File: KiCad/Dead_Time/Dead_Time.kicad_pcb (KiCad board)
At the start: 2 copper layers, 13 parts, among them Q7 PNP_BC558, U1 74AUC2G04, U2 Opamp_Dual

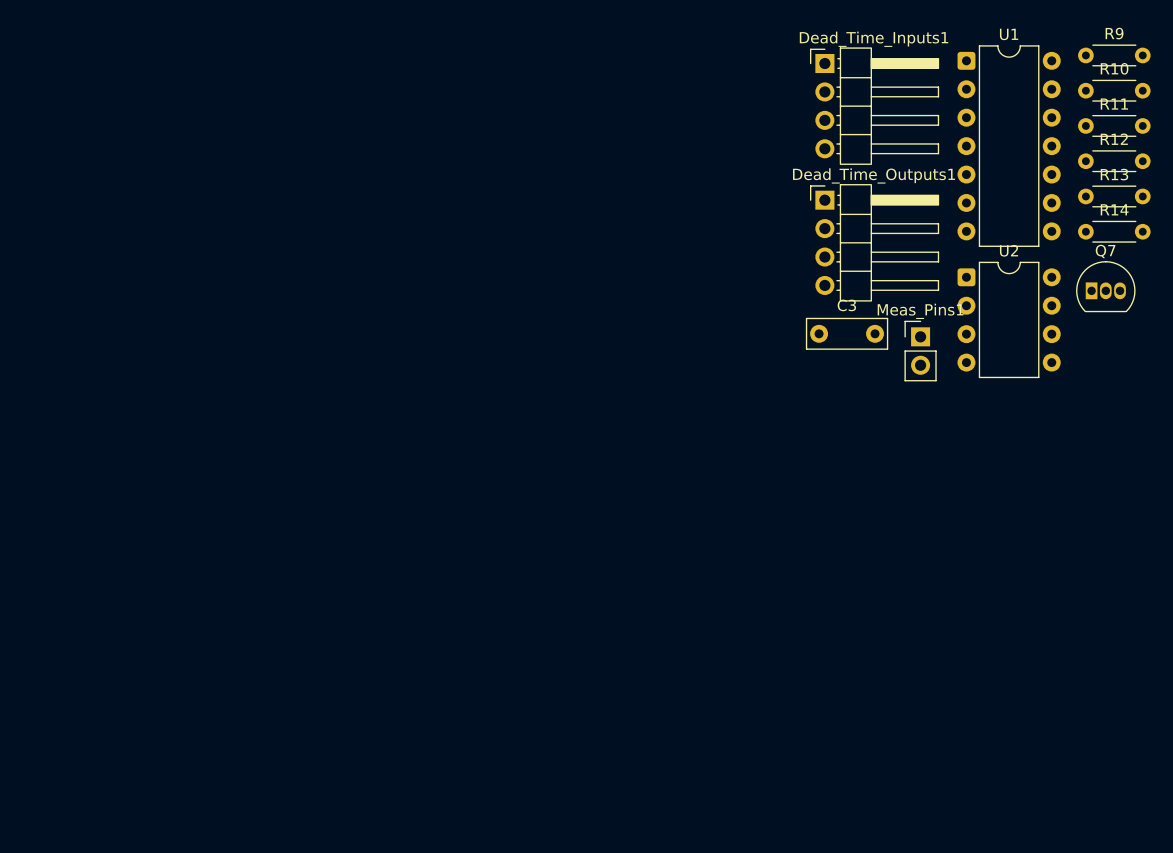
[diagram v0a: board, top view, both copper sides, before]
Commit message: deadtime pcb almost done, missing 1 gnd connection
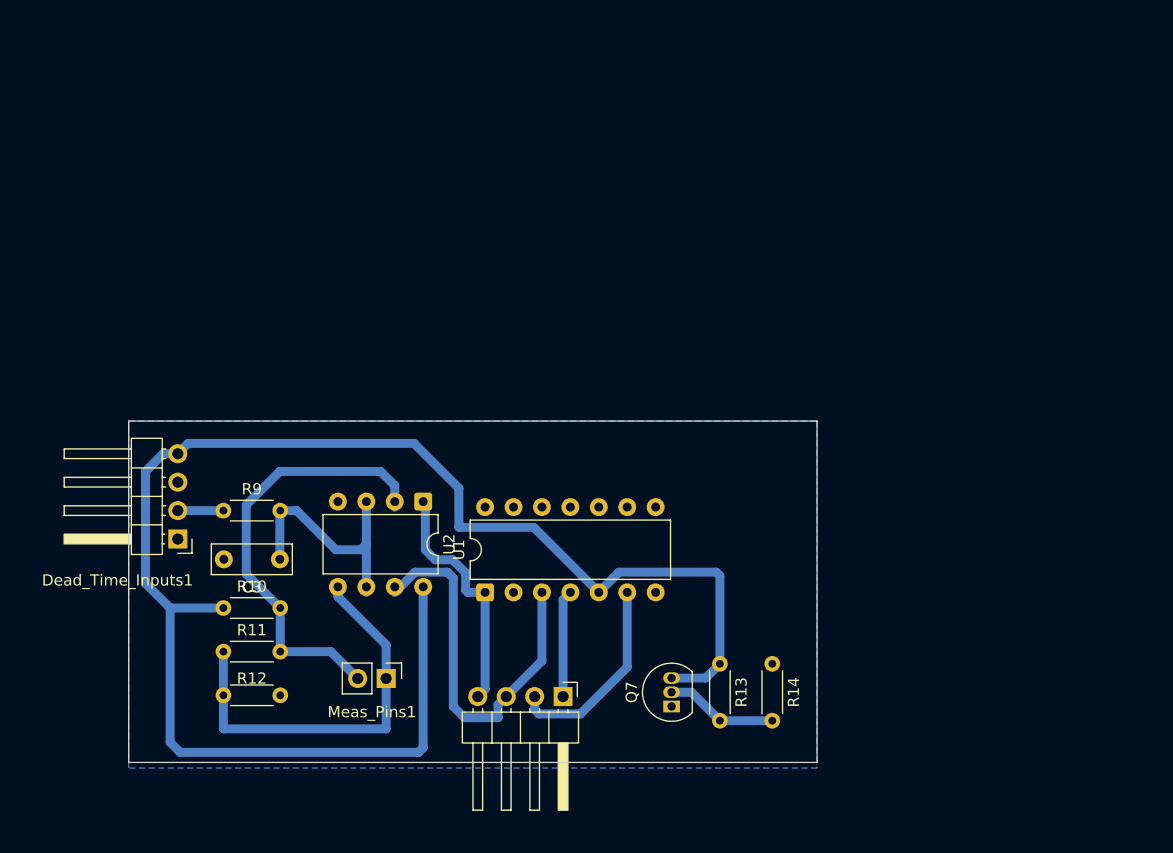
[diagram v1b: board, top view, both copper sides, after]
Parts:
- U2: value Opamp_Dual -> MCP6002
- moved R11 90.2 mm to (85.5, 118.6)
- moved R10 89.9 mm to (85.5, 114.7)
- moved R9 87.1 mm to (85.5, 106.0)
- moved R12 86.4 mm to (90.5, 122.5), turned to 180 degrees
- moved Dead_Time_Inputs1 71.7 mm to (81.4, 108.5), turned to 180 degrees
- moved U1 64.1 mm to (108.8, 113.3), turned to 90 degrees
- moved Meas_Pins1 56.7 mm to (100.0, 121.0), turned to -90 degrees
- moved R13 53.0 mm to (129.8, 119.7), turned to -90 degrees
- moved Q7 52.8 mm to (125.5, 123.5), turned to 90 degrees
- moved U2 52.5 mm to (103.3, 105.2), turned to -90 degrees
- moved C3 52.2 mm to (90.5, 110.3), turned to 180 degrees
- moved Dead_Time_Outputs1 50.1 mm to (115.8, 122.6), turned to -90 degrees
- moved R14 47.7 mm to (134.5, 119.7), turned to -90 degrees
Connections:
- U2 pad 4: (no net) -> GND
- U2 pad 8: (no net) -> +5V
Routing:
- net +5V: track 0.00 -> 140.9 mm
- net /Meas_VStep1: track 0.00 -> 39.2 mm
- net /Meas_VStep2: track 0.00 -> 35.8 mm
- net /PWM2: track 0.00 -> 34.9 mm
- net /PWM1: track 0.00 -> 21.5 mm
- net Net-(U2A-+): track 0.00 -> 21.3 mm
- net /PWM1_NOT: track 0.00 -> 18.0 mm
- net Net-(Q7-B): track 0.00 -> 10.1 mm
- net /PWM2_NOT: track 0.00 -> 9.58 mm
- net /PWM_In: track 0.00 -> 4.46 mm
- added copper zone on B.Cu, net GND
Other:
- board outline added: 61.5 x 30.5 mm

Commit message: gemme punkt før jeg laver om i deadtime pcb
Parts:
- moved Dead_Time_Inputs1 28.9 mm to (108.8, 99.6), turned to 90 degrees
- moved Dead_Time_Outputs1 0.65 mm to (116.5, 122.6)
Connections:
- Dead_Time_Inputs1 pad 1: /on_off -> /PWM_In
- Dead_Time_Inputs1 pad 2: /PWM_In -> GND
- Dead_Time_Inputs1 pad 3: GND -> +5V
- Dead_Time_Inputs1 pad 4: +5V -> /on/off
- U2 pad 8: +5V -> /KILL_SWITCH
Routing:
- net +5V: track 140.9 -> 100.5 mm
- net /KILL_SWITCH: track 0.00 -> 37.7 mm
- net /on/off: track 0.00 -> 33.5 mm
- net /PWM_In: track 4.46 -> 27.0 mm
- net /PWM2: track 34.9 -> 39.8 mm
- net /Meas_VStep2: track 35.8 -> 33.4 mm
- net /PWM1_NOT: track 18.0 -> 20.4 mm
- net /PWM1: track 21.5 -> 19.4 mm
- net Net-(U2A-+): track 21.3 -> 20.8 mm
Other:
- board size 61.5 x 30.5 mm -> 61.5 x 39.2 mm

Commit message: pcb layouts done
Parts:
- removed Meas_Pins1: Conn_01x02_Pin, Connector_PinHeader_2.54mm:PinHeader_1x02_P2.54mm_Vertical
- moved R14 40.1 mm to (94.8, 124.8), turned to 90 degrees
- moved R13 32.0 mm to (98.2, 124.8), turned to 90 degrees
- moved Q7 22.7 mm to (102.8, 122.2), turned to -90 degrees
- moved U1 15.4 mm to (123.9, 109.9), turned to -90 degrees
- moved R10 12.1 mm to (87.0, 102.7), turned to -90 degrees
- moved C3 10.0 mm to (82.8, 116.7), turned to -90 degrees
- moved Dead_Time_Inputs1 6.12 mm to (103.5, 102.7)
- moved U2 4.71 mm to (102.8, 109.9)
- moved R12 4.22 mm to (87.0, 124.8), turned to 90 degrees
- moved R9 3.20 mm to (82.8, 107.7), turned to -90 degrees
- moved R11 2.78 mm to (87.0, 116.3), turned to 90 degrees
- moved Dead_Time_Outputs1 1.56 mm to (116.2, 121.1)
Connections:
- Dead_Time_Inputs1 pad 1: /PWM_In -> +5V
- Dead_Time_Inputs1 pad 2: GND -> /PWM_In
- Dead_Time_Inputs1 pad 3: +5V -> GND
- Dead_Time_Outputs1 pad 1: /PWM2_NOT -> /PWM1
- Dead_Time_Outputs1 pad 4: /PWM1 -> /PWM2_NOT
- U1 pad 1: /PWM1 -> (no net)
- U1 pad 10: (no net) -> /PWM1_NOT
- U1 pad 11: (no net) -> /PWM1
- U1 pad 14: (no net) -> +5V
- U1 pad 2: GND -> (no net)
- U1 pad 3: /PWM2 -> (no net)
- U1 pad 4: /PWM2_NOT -> (no net)
- U1 pad 5: +5V -> (no net)
- U1 pad 6: /PWM1_NOT -> (no net)
- U1 pad 7: (no net) -> GND
- U1 pad 8: (no net) -> /PWM2_NOT
- U1 pad 9: (no net) -> /PWM2
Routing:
- net /on/off: track 33.5 -> 67.3 mm
- net /KILL_SWITCH: track 37.7 -> 4.75 mm
- net /PWM2: track 39.8 -> 16.9 mm
- net /Meas_VStep2: track 33.4 -> 11.7 mm
- net /Meas_VStep1: track 38.8 -> 19.2 mm
- net /PWM1_NOT: track 20.4 -> 3.50 mm
- net /PWM2_NOT: track 9.31 -> 3.50 mm
- net +5V: track 100.5 -> 94.9 mm
- net Net-(U2A-+): track 20.8 -> 26.0 mm
- net /PWM_In: track 27.0 -> 31.0 mm
- net /PWM1: track 19.4 -> 22.6 mm
- net Net-(Q7-B): track 10.1 -> 10.8 mm
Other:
- board size 61.5 x 39.2 mm -> 52.5 x 36.5 mm
